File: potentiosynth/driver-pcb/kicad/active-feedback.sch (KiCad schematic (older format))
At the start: 9 parts, among them U1 LM358

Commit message: first draft driver-pcb
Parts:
- removed QD1: IRF630, Package_TO_SOT_THT:TO-220-3_Vertical, symbol IRF630:IRF630
- removed QE1: 2N7000, Package_TO_SOT_THT:TO-92_Inline, symbol Transistor_FET:2N7000
- removed RL6: 10, Resistor_SMD:R_1206_3216Metric, symbol Device:R_US
- removed RV1: 2k, Potentiometer_THT:Potentiometer_Bourns_3296X_Horizontal, symbol Device:R_POT_TRIM_US
- removed U1: LM358, Package_DIP:DIP-8_W7.62mm_LongPads, symbol LM358:LM358
- added QE1: Q_NMOS_GSD, Package_TO_SOT_SMD:SOT-23_Handsoldering, symbol Device:Q_NMOS_GSD
- added RV1: R_POT_US, Potentiometer_THT:Potentiometer_Bourns_3296X_Horizontal, symbol Device:R_POT_US
- added U1: TLV9152IDR, Package_SO:SOIC-8_3.9x4.9mm_P1.27mm, symbol TLV9152IDR:TLV9152IDR
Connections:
- net labels added: COUNTER, REFERENCE
- net labels removed: CONTROL, RETURN, SUPPLY
- wire segments 34 -> 23
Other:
- note removed: "CONSTANT CURRENT DRIVER\nI = V_CONTROL / RV"
- moved on the sheet: R+6, R-6, RF6, RG6

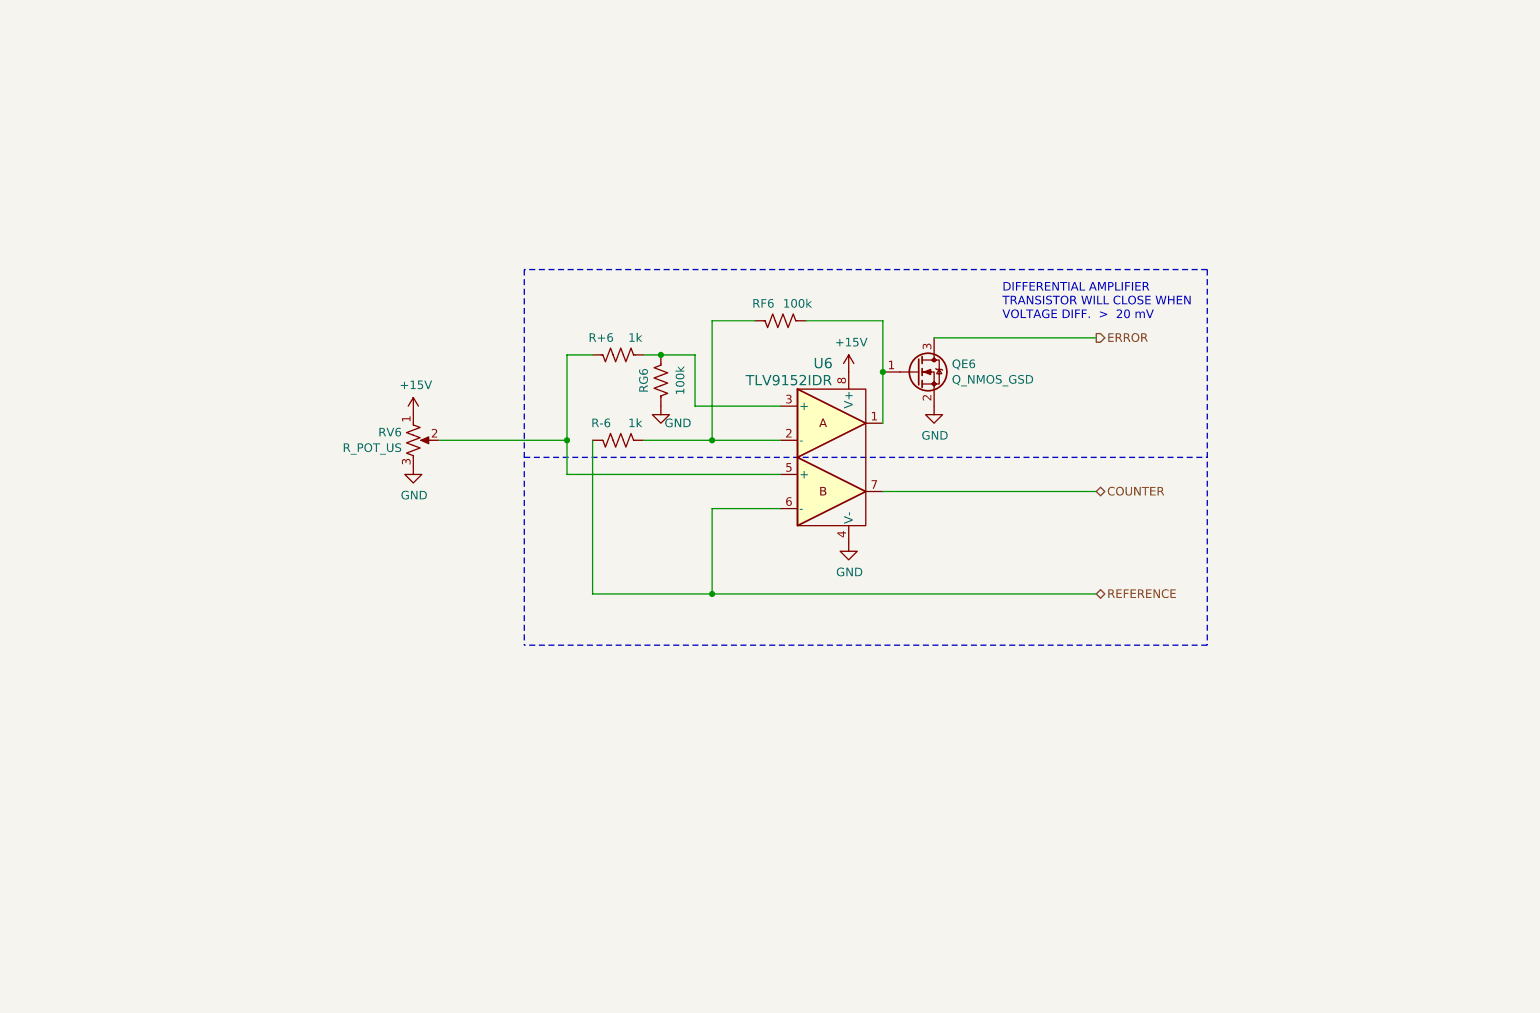
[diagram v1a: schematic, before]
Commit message: added buffer amplifier
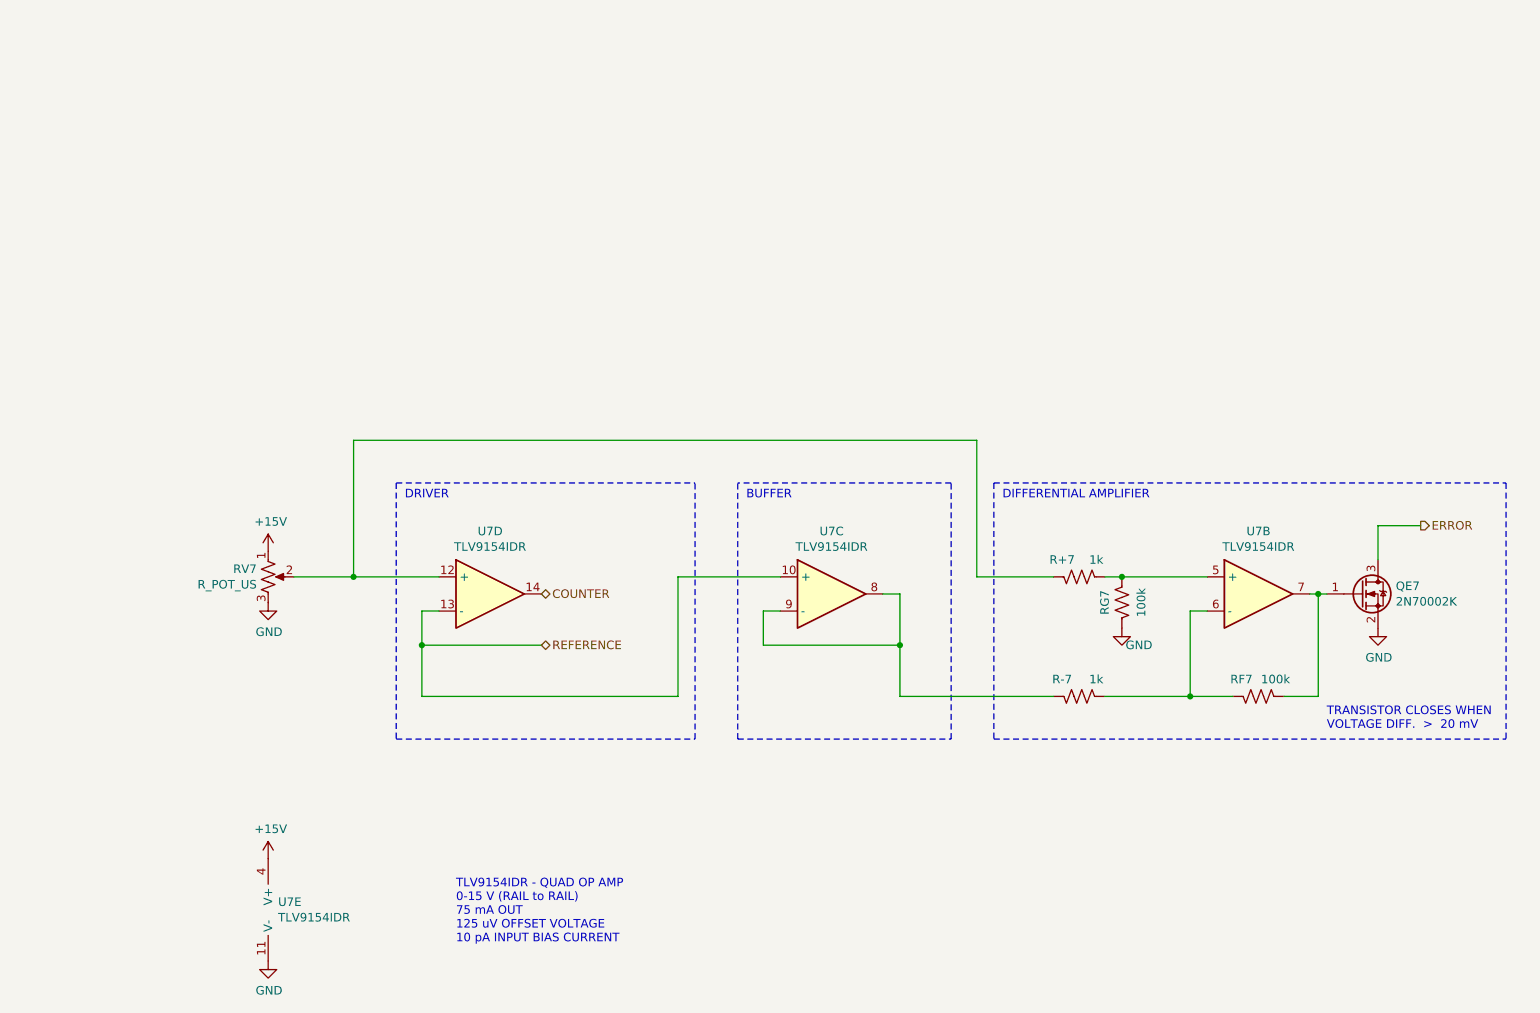
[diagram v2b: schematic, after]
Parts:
- removed U1: TLV9152IDR, Package_SO:SOIC-8_3.9x4.9mm_P1.27mm, symbol TLV9152IDR:TLV9152IDR
- added U1: TLV9154IDR, Package_SO:SOIC-14_3.9x8.7mm_P1.27mm, symbol Device:Opamp_Quad_Generic
- QE1: value Q_NMOS_GSD -> 2N70002K
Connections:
- net +15V: now also U1.4 (V+)
- net COUNTER: now also U1.14
- net GND: now also U1.11 (V-)
- net REFERENCE: now also U1.10 (+), U1.13 (-); no longer R-1.2
- net at R-1.1, RF1.1: now also U1.6 (-)
- net at QE1.1 (G), RF1.2: now also U1.7
- net at R+1.1, RV1.2: now also U1.12 (+)
- net at R+1.2, RG1.1: now also U1.5 (+)
- new net: R-1.2, U1.8, U1.9 (-)
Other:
- note added: "BUFFER"
- note added: "DIFFERENTIAL AMPLIFIER"
- note added: "DRIVER"
- note added: "TLV9154IDR - QUAD OP AMP\n0-15 V (RAIL to RAIL)\n75 mA OUT\n125 uV OFFSET VOLTAGE\n10 pA INPUT BIAS CURRENT"
- note added: "TRANSISTOR CLOSES WHEN\nVOLTAGE DIFF. > 20 mV"
- note removed: "DIFFERENTIAL AMPLIFIER\nTRANSISTOR WILL CLOSE WHEN\nVOLTAGE DIFF. > 20 mV"
- moved on the sheet: QE7, R+7, R-7, RF7, RG7, RV7

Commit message: resistor net
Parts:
- removed R+1, R-1: 1k, Resistor_SMD:R_1206_3216Metric, symbol Device:R_US
- removed RF1, RG1: 100k, Resistor_SMD:R_1206_3216Metric, symbol Device:R_US
- added C7: C, symbol Device:C
- added QEN1: 2N70002K, Package_TO_SOT_SMD:SOT-23_Handsoldering, symbol Device:Q_NMOS_GSD
- added RNH1: 100k, footprints:CAY16-104J4LF, symbol r_pack04_split_us:R_Pack04_Split_US
- added RNL1: 1k, footprints:CAY16-104J4LF, symbol r_pack04_split_us:R_Pack04_Split_US
- added unit 1 of U1
- RV1: value R_POT_US -> 2k
- renumbered QE1 to QEP1
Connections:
- net ERROR: now also QEN1.3 (D)
- net GND: now also C7.2, QEN1.2 (S), RNH1.5 (R4.2), RNH1.6 (R3.2)
- net REFERENCE: now also C7.1
- net at U1.6 (-): now also RNH1.8 (R1.2), RNL1.7 (R2.2)
- net at QEP1.1 (G), U1.7: now also RNH1.1 (R1.1)
- net at U1.8, U1.9 (-): now also RNL1.2 (R2.1), RNL1.3 (R3.1)
- net at RV1.2, U1.12 (+): now also RNL1.1 (R1.1), RNL1.4 (R4.1)
- net at U1.5 (+): now also RNH1.3 (R3.1), RNL1.8 (R1.2)
- new net: QEN1.1 (G), RNH1.7 (R2.2), U1.1
- new net: RNH1.2 (R2.1), RNL1.5 (R4.2), U1.2 (-)
- new net: RNH1.4 (R4.1), RNL1.6 (R3.2), U1.3 (+)
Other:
- note added: "NEGATIVE DIFFERENTIAL AMPLIFIER"
- note added: "POSITIVE DIFFERENTIAL AMPLIFIER"
- note added: "TRANSISTOR CLOSES WHEN\nVOLTAGE DIFF. < 20 mV"
- note removed: "DIFFERENTIAL AMPLIFIER"
- moved on the sheet: QEP2, RV2, U2B, U2C, U2D, U2E

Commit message: potentiosynth driver revC
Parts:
- C1: renamed from C7; footprint (none) -> Capacitor_SMD:C_1206_3216Metric_Pad1.33x1.80mm_HandSolder
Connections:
- net at RNL1.1 (R1.1), RV1.2, U1.12 (+): now also RNL1.2 (R2.1); no longer RNL1.4 (R4.1)
- net at RNL1.3 (R3.1), U1.8, U1.9 (-): now also RNL1.4 (R4.1); no longer RNL1.2 (R2.1)
- net at RNH1.8 (R1.2), U1.6 (-): now also RNL1.5 (R4.2); no longer RNL1.7 (R2.2)
- net at RNH1.2 (R2.1), U1.2 (-): now also RNL1.7 (R2.2); no longer RNL1.5 (R4.2)
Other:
- moved on the sheet: C1, RNL1B, RNL1D
